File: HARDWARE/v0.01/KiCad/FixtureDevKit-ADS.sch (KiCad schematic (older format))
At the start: 54 parts, among them J31 ADS_0, J32 ADS_1, J33 ADS, J34 ADS 0, J35 ADS1, J36 ADS, J37 ADS0, J38 ADS1, J39 ADS_2, J40 ADS_3, J41 ADS3, J42 ADS3, J43 ADS3, J44 ADS3, U5 ADS1015IDGST, U6 ADS1015IDGST, U7 ADS1015IDGST, U8 ADS1015IDGST

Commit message: adding some comments for Howie
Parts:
- J31: value ADS_0 -> ADS_48
- J32: value ADS_1 -> ADS_49
- J34: value ADS 0 -> ADS_48
- J35, J38: value ADS1 -> ADS_49
- J37: value ADS0 -> ADS_48
- J39: value ADS_2 -> ADS_4A
- J40: value ADS_3 -> ADS_4B
- J41, J43: value ADS3 -> ADS_4A
- J42, J44: value ADS3 -> ADS_4B
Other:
- note added: "ADS_48"
- note added: "ADS_49\n"
- note added: "ADS_4A"
- note added: "ADS_4B\n"
- note removed: "ADS_0\n"
- note removed: "ADS_1"
- note removed: "ADS_2"
- note removed: "ADS_3"
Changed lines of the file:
@@
 LIBS:contrib
 LIBS:valves
+LIBS:FDN337N
 LIBS:Fixture-Dev-Kit-cache
 EELAYER 25 0
@@
 $Descr A4 11693 8268
 encoding utf-8
-Sheet 4 9
+Sheet 4 10
 Title ""
 Date ""
@@
 P 3350 2300
 F 0 "J34" H 3350 2500 50  0000 C CNN
-F 1 "ADS 0" H 3350 2000 50  0000 C CNN
+F 1 "ADS_48" H 3350 2000 50  0000 C CNN
 F 2 "" H 3350 2300 50  0001 C CNN
 F 3 "" H 3350 2300 50  0001 C CNN
@@
 P 1450 1450
 F 0 "J31" H 1450 1650 50  0000 C CNN
-F 1 "ADS_0" H 1450 1150 50  0000 C CNN
+F 1 "ADS_48" H 1450 1150 50  0000 C CNN
 F 2 "" H 1450 1450 50  0001 C CNN
 F 3 "" H 1450 1450 50  0001 C CNN
@@
 P 1450 3500
 F 0 "J37" H 1450 3700 50  0000 C CNN
-F 1 "ADS0" H 1450 3200 50  0000 C CNN
+F 1 "ADS_48" H 1450 3200 50  0000 C CNN
 F 2 "" H 1450 3500 50  0001 C CNN
 F 3 "" H 1450 3500 50  0001 C CNN
@@
 	1550 3300 1550 3250
 Text Notes 650  1250 0    157  ~ 0
-ADS_0\n
+ADS_48
 Wire Notes Line
 	600  1000 3800 1000
@@
 P 6600 2300
 F 0 "J35" H 6600 2500 50  0000 C CNN
-F 1 "ADS1" H 6600 2000 50  0000 C CNN
+F 1 "ADS_49" H 6600 2000 50  0000 C CNN
 F 2 "" H 6600 2300 50  0001 C CNN
 F 3 "" H 6600 2300 50  0001 C CNN
@@
 P 4700 1450
 F 0 "J32" H 4700 1650 50  0000 C CNN
-F 1 "ADS_1" H 4700 1150 50  0000 C CNN
+F 1 "ADS_49" H 4700 1150 50  0000 C CNN
 F 2 "" H 4700 1450 50  0001 C CNN
 F 3 "" H 4700 1450 50  0001 C CNN
@@
 P 4700 3500
 F 0 "J38" H 4700 3700 50  0000 C CNN
-F 1 "ADS1" H 4700 3200 50  0000 C CNN
+F 1 "ADS_49" H 4700 3200 50  0000 C CNN
 F 2 "" H 4700 3500 50  0001 C CNN
 F 3 "" H 4700 3500 50  0001 C CNN
@@
 	4800 3300 4800 3250
 Text Notes 3900 1250 0    157  ~ 0
-ADS_1
+ADS_49\n
 Wire Notes Line
 	3850 1000 7050 1000
@@
 P 3350 5000
 F 0 "J41" H 3350 5200 50  0000 C CNN
-F 1 "ADS3" H 3350 4700 50  0000 C CNN
+F 1 "ADS_4A" H 3350 4700 50  0000 C CNN
 F 2 "" H 3350 5000 50  0001 C CNN
 F 3 "" H 3350 5000 50  0001 C CNN
@@
 P 1450 4150
 F 0 "J39" H 1450 4350 50  0000 C CNN
-F 1 "ADS_2" H 1450 3850 50  0000 C CNN
+F 1 "ADS_4A" H 1450 3850 50  0000 C CNN
 F 2 "" H 1450 4150 50  0001 C CNN
 F 3 "" H 1450 4150 50  0001 C CNN
@@
 P 1450 6200
 F 0 "J43" H 1450 6400 50  0000 C CNN
-F 1 "ADS3" H 1450 5900 50  0000 C CNN
+F 1 "ADS_4A" H 1450 5900 50  0000 C CNN
 F 2 "" H 1450 6200 50  0001 C CNN
 F 3 "" H 1450 6200 50  0001 C CNN
@@
 	1550 6000 1550 5950
 Text Notes 650  3950 0    157  ~ 0
-ADS_2
+ADS_4A
 Wire Notes Line
 	600  3700 3800 3700
@@
 P 6600 5000
 F 0 "J42" H 6600 5200 50  0000 C CNN
-F 1 "ADS3" H 6600 4700 50  0000 C CNN
+F 1 "ADS_4B" H 6600 4700 50  0000 C CNN
 F 2 "" H 6600 5000 50  0001 C CNN
 F 3 "" H 6600 5000 50  0001 C CNN
@@
 P 4700 4150
 F 0 "J40" H 4700 4350 50  0000 C CNN
-F 1 "ADS_3" H 4700 3850 50  0000 C CNN
+F 1 "ADS_4B" H 4700 3850 50  0000 C CNN
 F 2 "" H 4700 4150 50  0001 C CNN
 F 3 "" H 4700 4150 50  0001 C CNN
@@
 P 4700 6200
 F 0 "J44" H 4700 6400 50  0000 C CNN
-F 1 "ADS3" H 4700 5900 50  0000 C CNN
+F 1 "ADS_4B" H 4700 5900 50  0000 C CNN
 F 2 "" H 4700 6200 50  0001 C CNN
 F 3 "" H 4700 6200 50  0001 C CNN
@@
 	4800 6000 4800 5950
 Text Notes 3900 3950 0    157  ~ 0
-ADS_3
+ADS_4B\n
 Wire Notes Line
 	3850 3700 7050 3700

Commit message: updating the cover page
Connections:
- net SCL renamed I2C-SCK
- net SDA renamed I2C-SDA
- net VS renamed C4-VCC-3V3
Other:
- moved on the sheet: C5, C6, C7, C8, J31, J32, J33, J34, J35, J36, J37, J38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

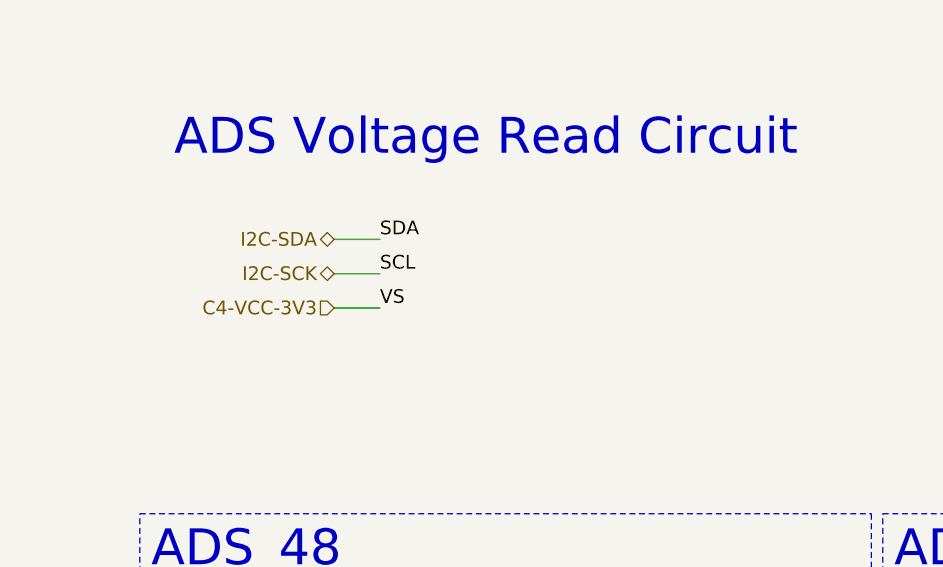
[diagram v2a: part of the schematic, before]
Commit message: adding labelings, hierarchy pins, and page titles
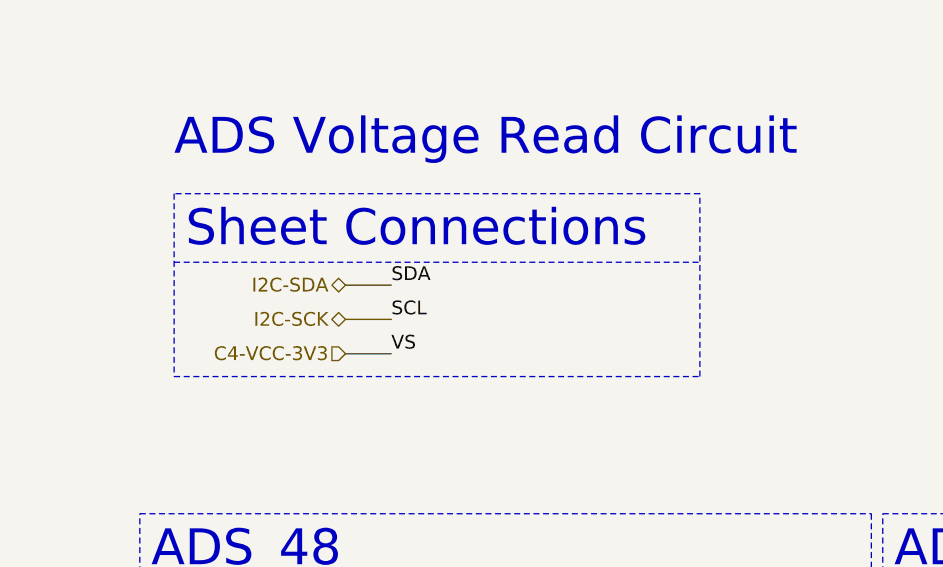
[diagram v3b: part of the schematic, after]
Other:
- note added: "Sheet Connections"
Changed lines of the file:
@@
 encoding utf-8
 Sheet 4 10
-Title ""
-Date ""
-Rev ""
-Comp ""
-Comment1 ""
+Title "ADS Circuits"
+Date "2017-10-25"
+Rev "v0.01"
+Comp "Next Thing Co"
+Comment1 "Havin' a Blast!"
 Comment2 ""
 Comment3 ""
@@
 Wire Wire Line
 	4000 7000 4000 7050
-Text HLabel 1350 1150 0    60   BiDi ~ 0
+Text HLabel 1400 1350 0    60   BiDi ~ 0
 I2C-SDA
-Text HLabel 1350 1300 0    60   BiDi ~ 0
+Text HLabel 1400 1500 0    60   BiDi ~ 0
 I2C-SCK
-Text HLabel 1350 1450 0    60   Input ~ 0
+Text HLabel 1400 1650 0    60   Input ~ 0
 C4-VCC-3V3
-Text Label 1550 1450 0    60   ~ 0
-VS
-Text Label 1550 1150 0    60   ~ 0
-SDA
-Text Label 1550 1300 0    60   ~ 0
-SCL
-Wire Wire Line
-	1350 1150 1550 1150
-Wire Wire Line
-	1550 1300 1350 1300
-Wire Wire Line
-	1350 1450 1550 1450
+Text Label 1600 1650 0    60   ~ 0
+VS
+Text Label 1600 1350 0    60   ~ 0
+SDA
+Text Label 1600 1500 0    60   ~ 0
+SCL
+Wire Wire Line
+	1400 1350 1600 1350
+Wire Wire Line
+	1600 1500 1400 1500
+Wire Wire Line
+	1400 1650 1600 1650
+Text Notes 700  1200 0    157  ~ 0
+Sheet Connections
+Wire Notes Line
+	650  950  650  1750
+Wire Notes Line
+	650  1750 2950 1750
+Wire Notes Line
+	2950 1750 2950 950
+Wire Notes Line
+	2950 950  650  950
+Wire Notes Line
+	650  1250 2950 1250
 $EndSCHEMATC

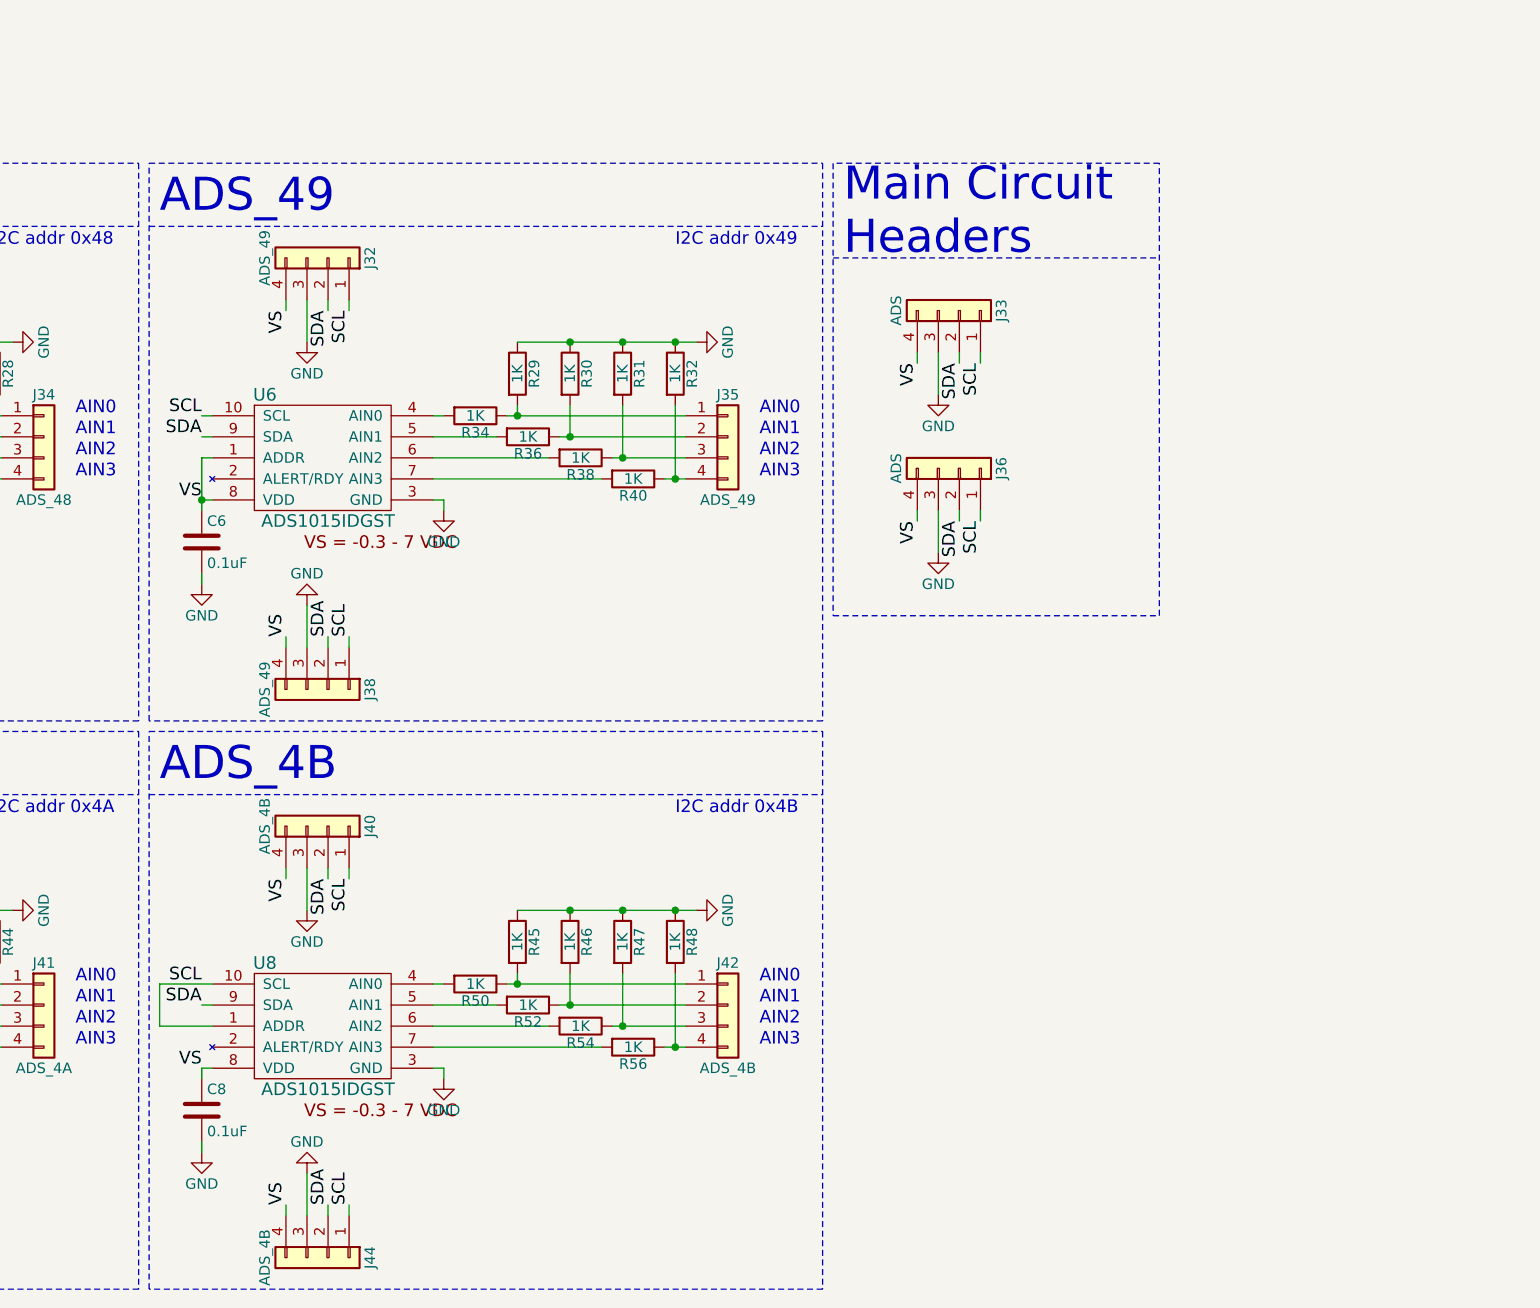
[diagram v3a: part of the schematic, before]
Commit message: adjusting page sizes and cleaning up schematics
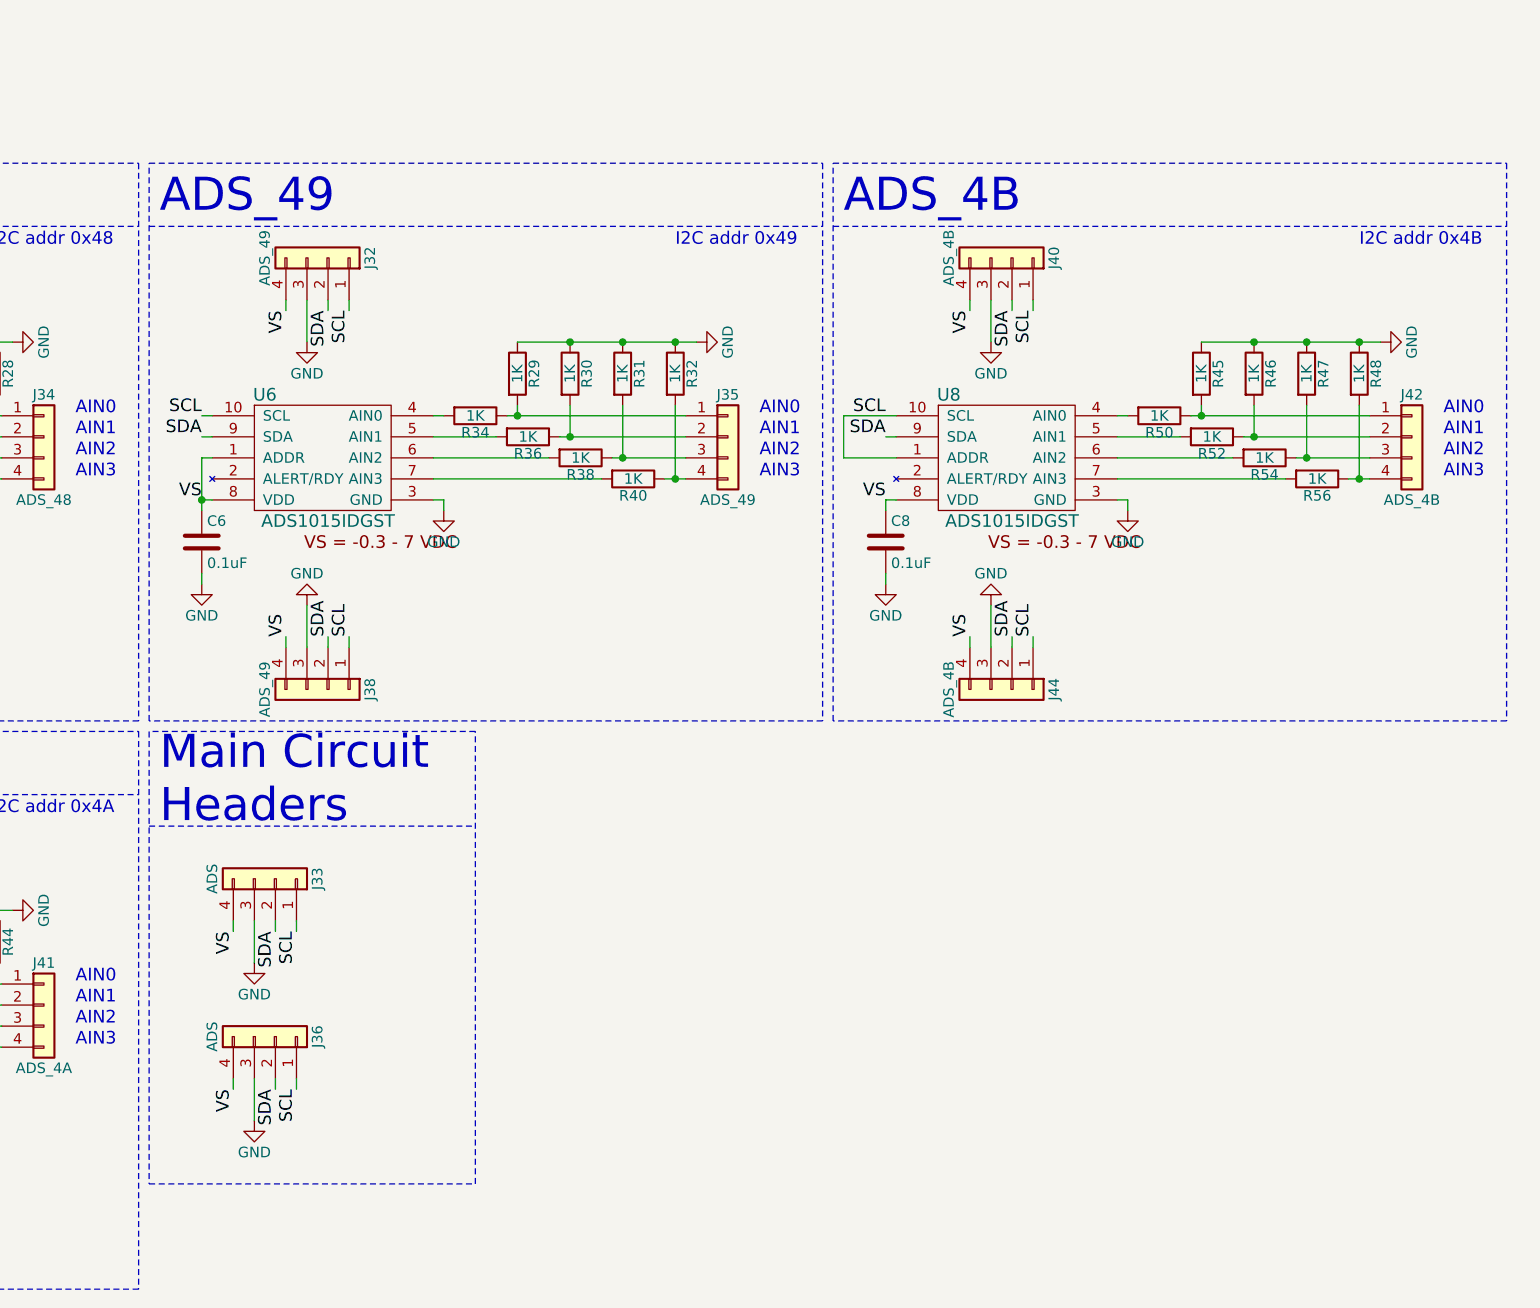
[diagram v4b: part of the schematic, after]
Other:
- moved on the sheet: C8, J33, J36, J40, J42, J44, R45, R46, R47, R48, R50, R52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

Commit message: cleaning up schematic, run rules check, generate net list
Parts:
- renumbered C5 to C1, C7 to C2, C6 to C3, C8 to C4, J31 to J16, J37 to J17, J39 to J18, J43 to J19, J34 to J20, J41 to J21, J33 to J22, J36 to J23, J32 to J24, J38 to J25, J35 to J26, J40 to J27, J44 to J28, J42 to J29, R33 to R13, R49 to R14, R25 to R15, R41 to R16, R35 to R17, R51 to R18, R26 to R19, R42 to R20, R37 to R21, R53 to R22, R27 to R23, R43 to R24, R39 to R25, R55 to R26, R28 to R27, R44 to R28, R34 to R29, R29 to R30, R36 to R31, R30 to R32, R38 to R33, R31 to R34, R40 to R35, R32 to R36, R50 to R37, R45 to R38, R52 to R39, R46 to R40, R54 to R41, R47 to R42, R56 to R43, R48 to R44, U5 to U1, U7 to U2, U6 to U3, U8 to U4
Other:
- note removed: "TO DO:\n- is it okay to have so many headers on the I2C lines?\n- Do we want the cut trace connector or not connect?\n- where do we want to add test points?\n- power-supply decoupling capacitor to GND. 0.1uF"

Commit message: adding footprints
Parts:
- C1, C2, C3, C4: footprint (none) -> Capacitors_SMD:C_0805_HandSoldering
- J16, J17, J18, J19, J20, J21, J22, J23, J24, J25, J26, J27, J28, J29: footprint (none) -> Pin_Headers:Pin_Header_Straight_1x04_Pitch2.54mm
- R13, R14, R15, R16, R17, R18, R19, R20, R21, R22, R23, R24, R25, R26, R27, R28, R29, R30, R31, R32, R33, R34, R35, R36, R37, R38, R39, R40, R41, R42, R43, R44: footprint (none) -> Resistors_SMD:R_0805_HandSoldering

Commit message: adding footprints, starting layout
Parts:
- U1, U2, U3, U4: footprint (none) -> ADS1015IDGST:SOP50P490X110-10N
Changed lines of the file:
@@
 LIBS:contrib
 LIBS:valves
-LIBS:FDN337N
+LIBS:TCA6424ARGJR
 LIBS:Fixture-Dev-Kit-cache
 EELAYER 25 0
@@
 F 0 "U1" H 1050 4650 60  0000 C CNN
 F 1 "ADS1015IDGST" H 1350 4050 60  0000 C CNN
-F 2 "" H 1350 4050 60  0001 C CNN
+F 2 "ADS1015IDGST:SOP50P490X110-10N" H 1350 4050 60  0001 C CNN
 F 3 "" H 1350 4050 60  0001 C CNN
 	1    1350 4050
@@
 F 0 "U3" H 4300 4650 60  0000 C CNN
 F 1 "ADS1015IDGST" H 4600 4050 60  0000 C CNN
-F 2 "" H 4600 4050 60  0001 C CNN
+F 2 "ADS1015IDGST:SOP50P490X110-10N" H 4600 4050 60  0001 C CNN
 F 3 "" H 4600 4050 60  0001 C CNN
 	1    4600 4050
@@
 F 0 "U2" H 1050 7350 60  0000 C CNN
 F 1 "ADS1015IDGST" H 1350 6750 60  0000 C CNN
-F 2 "" H 1350 6750 60  0001 C CNN
+F 2 "ADS1015IDGST:SOP50P490X110-10N" H 1350 6750 60  0001 C CNN
 F 3 "" H 1350 6750 60  0001 C CNN
 	1    1350 6750
@@
 F 0 "U4" H 7550 4650 60  0000 C CNN
 F 1 "ADS1015IDGST" H 7850 4050 60  0000 C CNN
-F 2 "" H 7850 4050 60  0001 C CNN
+F 2 "ADS1015IDGST:SOP50P490X110-10N" H 7850 4050 60  0001 C CNN
 F 3 "" H 7850 4050 60  0001 C CNN
 	1    7850 4050
